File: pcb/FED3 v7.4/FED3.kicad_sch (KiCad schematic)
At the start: 29 parts, among them IC2 TB6612FNG, SW1 Sw, U2 MIC5504-3.3, U3 MCP73831T, X5 JST-XH-02

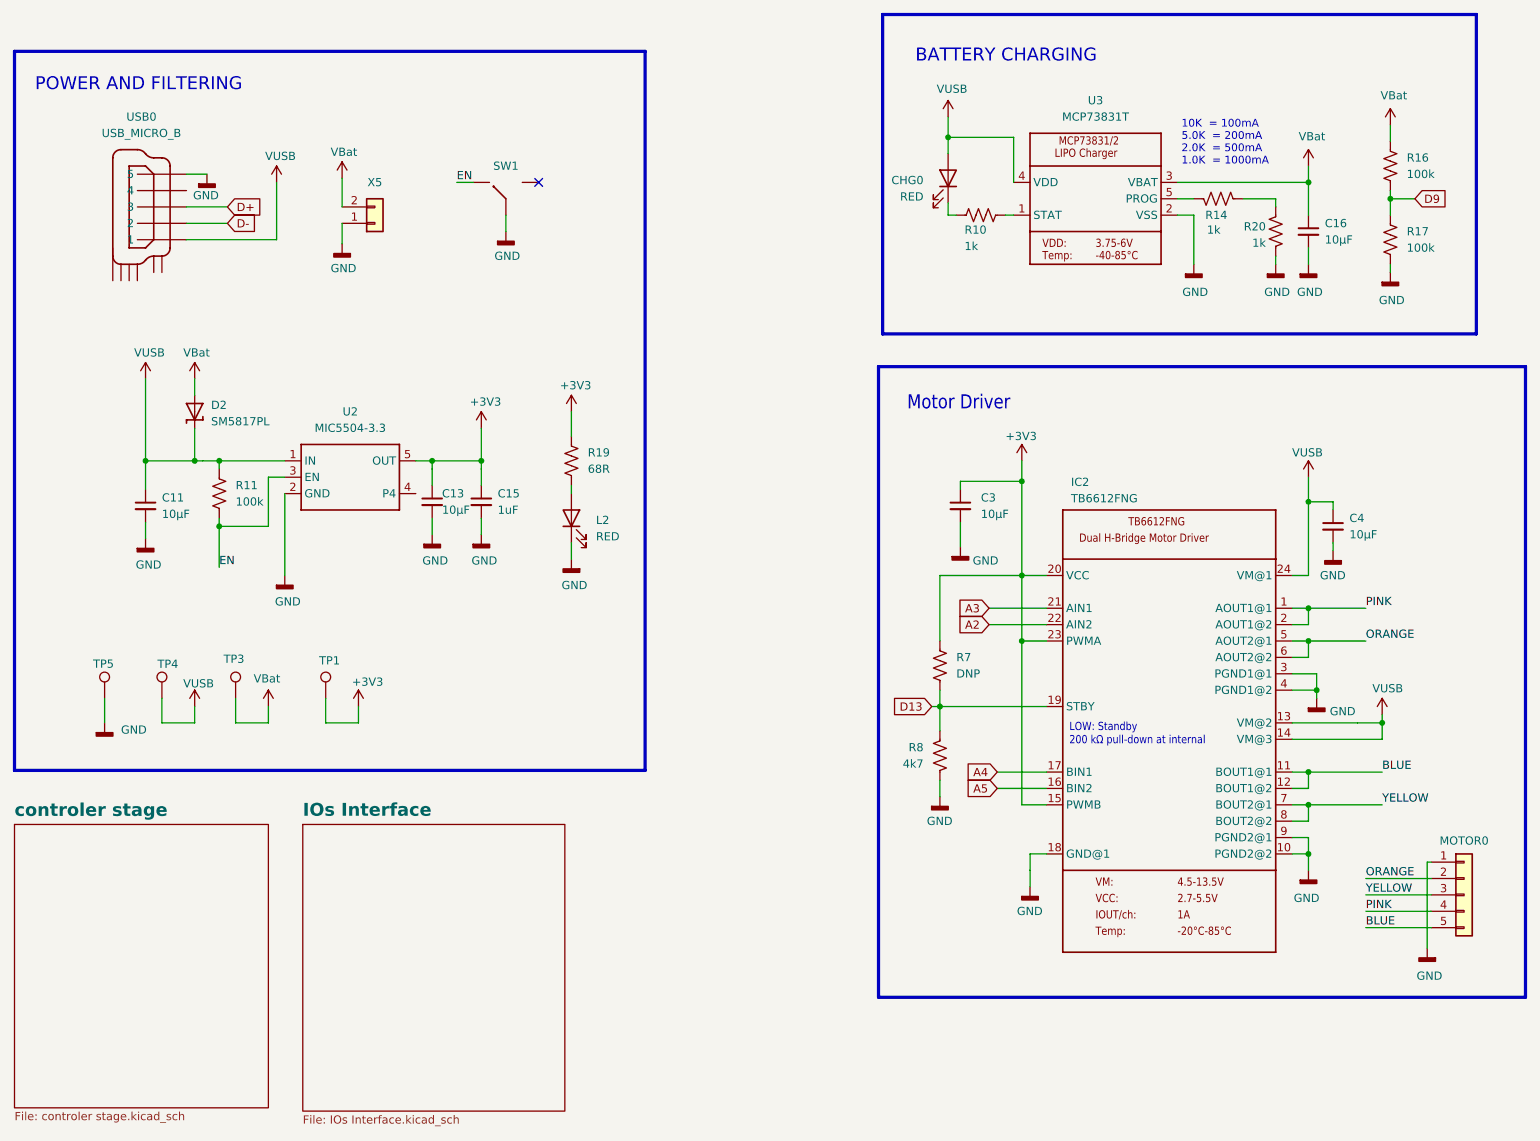
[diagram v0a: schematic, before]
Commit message: v.7.4 - alterações rail power
v.7.4
- modificada estrutura rail power: VUSB apenas para Vcharging
- modificadas Rs de LEDs para diminuir I
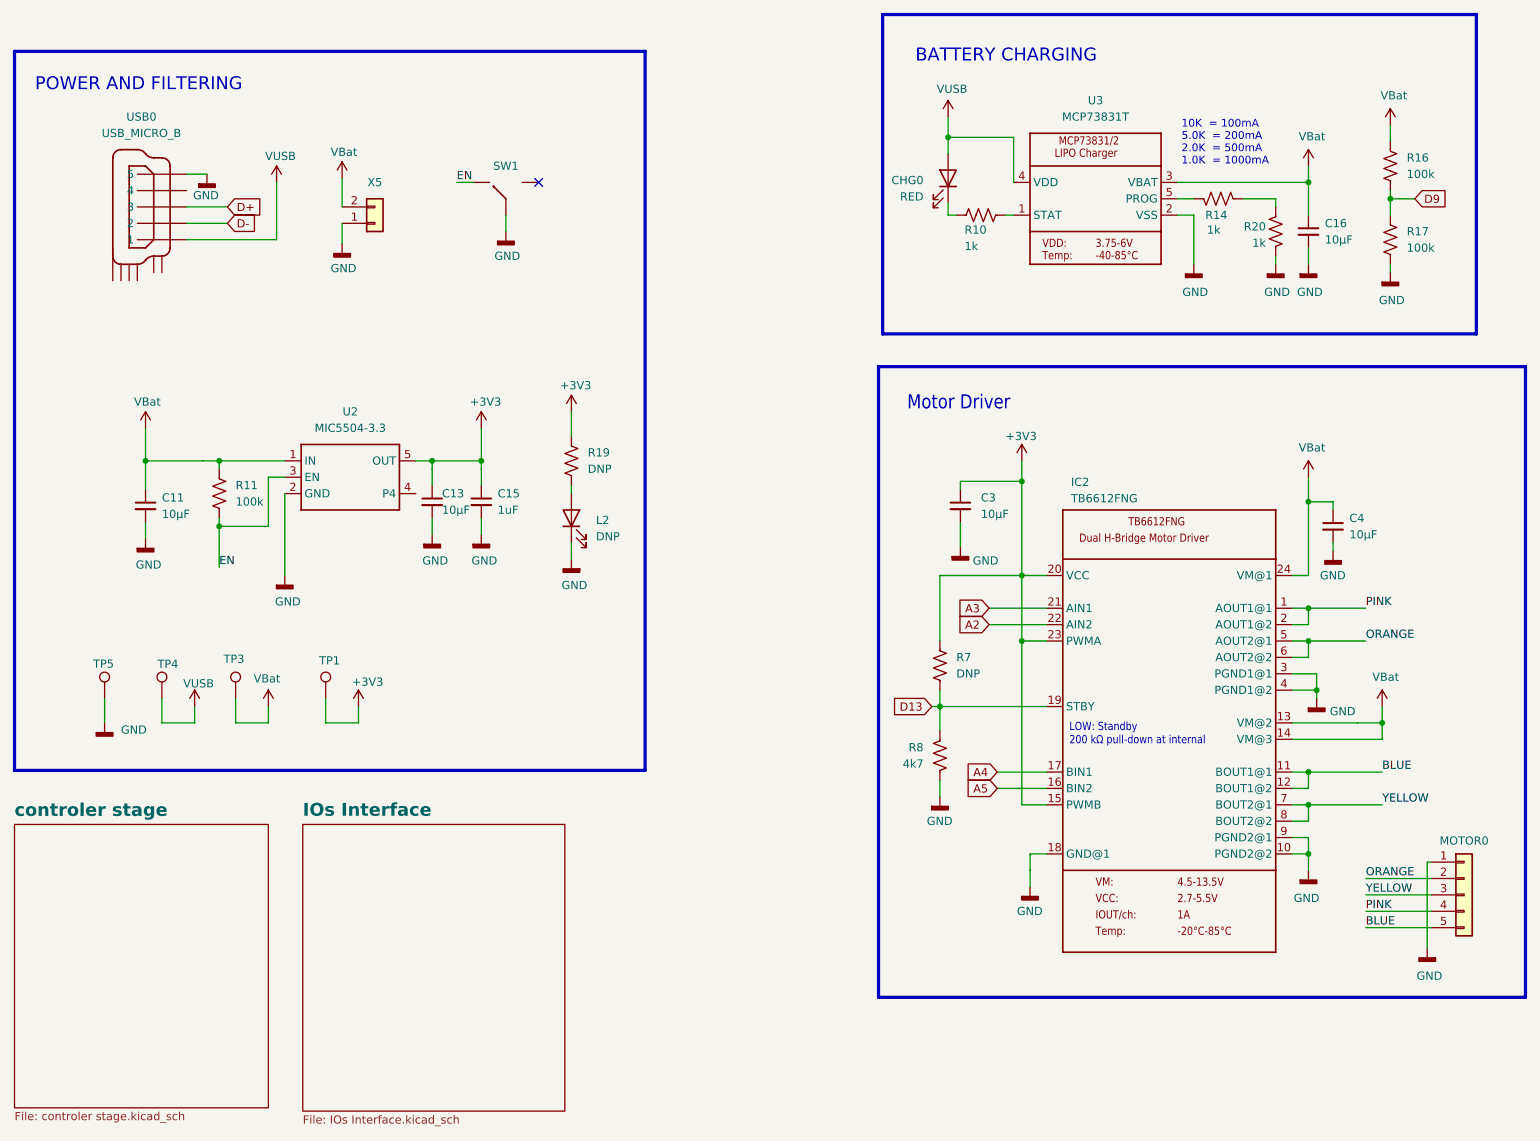
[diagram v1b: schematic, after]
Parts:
- removed D2: SM5817PL, Diode_SMD:D_SOD-123F, symbol FED3 SymbLib:DIODE-SCHOTTKYSOD-123
- L2: value RED -> DNP; MPN 5975004407F -> n.a.; OEPSPN OEPS030006 -> n.a.
- R16, R17: MPN ERJ-2RKF1003X -> RG1005P-104-B-T5; OEPSPN OEPS020019 -> OEPS020175
- R19: value 68R -> DNP; MPN RCS040268R0FKED -> n.a.; OEPSPN OEPS020032 -> n.a.; now left out of the parts list
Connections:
- net VBat: now also C11.1, C4.1, IC2.13 (VM@2), IC2.14 (VM@3), IC2.24 (VM@1), R11.1, U2.1 (IN)
- net VUSB: no longer C11.1, C4.1, IC2.13 (VM@2), IC2.14 (VM@3), IC2.24 (VM@1), R11.1, U2.1 (IN)

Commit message: v.7.4 - commit to final review
- I2C plug moved to board front side
- Rs to LEDs changed - impose less I
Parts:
- R11: MPN ERJ-2RKF1003X -> RG1005P-104-B-T5; OEPSPN OEPS020019 -> OEPS020175
- TP5: now left out of the parts list
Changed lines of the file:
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@@
 			)
 		)
-		(property "Description" ""
+		(property "Description" "SMD 0402 100kΩ ±0.1% 0.063W"
 			(at 58.42 88.9 0)
 			(effects
@@
 			)
 		)
-		(property "OEPSPN" "OEPS020019"
+		(property "OEPSPN" "OEPS020175"
 			(at 58.42 88.9 0)
 			(effects
@@
 			)
 		)
-		(property "MPN" "ERJ-2RKF1003X"
+		(property "MPN" "RG1005P-104-B-T5"
 			(at 58.42 88.9 0)
 			(effects
@@
 			)
 		)
-		(property "Description" ""
+		(property "Description" "LDO 3.3V 300mA"
 			(at 78.74 86.36 0)
 			(effects
@@
 			)
 		)
-		(property "Description" ""
+		(property "Description" "SMD CER 0402 1uF 25V ±10% X5R"
 			(at 99.06 90.17 0)
 			(effects
@@
 			)
 		)
-		(property "Description" ""
+		(property "Description" "SMD 0402 1kΩ ±1% 0.100W"
 			(at 213.36 43.18 0)
 			(effects
@@
 		(unit 1)
 		(exclude_from_sim no)
-		(in_bom yes)
+		(in_bom no)
 		(on_board yes)
 		(dnp no)
@@
 			)
 		)
-		(property "Description" ""
+		(property "Description" "SMD 0402 4.7kΩ ±1% 0.100W"
 			(at 170.18 129.54 0)
 			(effects
@@
 			)
 		)
-		(property "Description" ""
+		(property "Description" "BATT CNTL LI-ION 1CEL"
 			(at 194.31 43.18 0)
 			(effects
@@
 			)
 		)
-		(property "Description" ""
+		(property "Description" "SWITCH SLIDE SPDT 0.3A 5V (OEPS K01 017)"
 			(at 102.87 40.64 0)
 			(effects
@@
 			)
 		)
-		(property "Description" ""
+		(property "Description" "SMD 0402 1kΩ ±1% 0.100W"
 			(at 222.25 48.26 0)
 			(effects
@@
 			)
 		)
-		(property "Description" ""
+		(property "Description" "MOTOR DRIVER 2.7V-5.5V (OEPS K01 002)"
 			(at 204.47 124.46 0)
 			(effects
@@
 			)
 		)
-		(property "Description" ""
+		(property "Description" "SMD 0402 100kΩ ±0.1% 0.063W"
 			(at 240.03 38.1 0)
 			(effects
@@
 			)
 		)
-		(property "Description" ""
+		(property "Description" "SMD 0402 1kΩ ±1% 0.100W"
 			(at 176.53 45.72 0)
 			(effects
@@
 			)
 		)
-		(property "Description" ""
+		(property "Description" "SMD 0402 100kΩ ±0.1% 0.063W"
 			(at 240.03 49.53 0)
 			(effects

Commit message: FED3 v7.3 - 2nd revision
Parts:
- L2, R7: now not fitted; now left out of the parts list
- R11, R16, R17: value 100k -> 100k 0.1%
- R19: now not fitted
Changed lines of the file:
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@@
 			)
 		)
-		(property "Value" "100k"
+		(property "Value" "100k 0.1%"
 			(at 60.96 90.1699 0)
 			(effects
@@
 		(unit 1)
 		(exclude_from_sim no)
-		(in_bom yes)
+		(in_bom no)
 		(on_board yes)
-		(dnp no)
+		(dnp yes)
 		(fields_autoplaced yes)
 		(property "Reference" "L2"
@@
 		(in_bom no)
 		(on_board yes)
-		(dnp no)
+		(dnp yes)
 		(fields_autoplaced yes)
 		(property "Reference" "R19"
@@
 			)
 		)
-		(property "Value" "100k"
+		(property "Value" "100k 0.1%"
 			(at 242.57 39.3699 0)
 			(effects
@@
 			)
 		)
-		(property "Value" "100k"
+		(property "Value" "100k 0.1%"
 			(at 242.57 50.7999 0)
 			(effects
@@
 		(unit 1)
 		(exclude_from_sim no)
-		(in_bom yes)
+		(in_bom no)
 		(on_board yes)
-		(dnp no)
+		(dnp yes)
 		(fields_autoplaced yes)
 		(property "Reference" "R7"

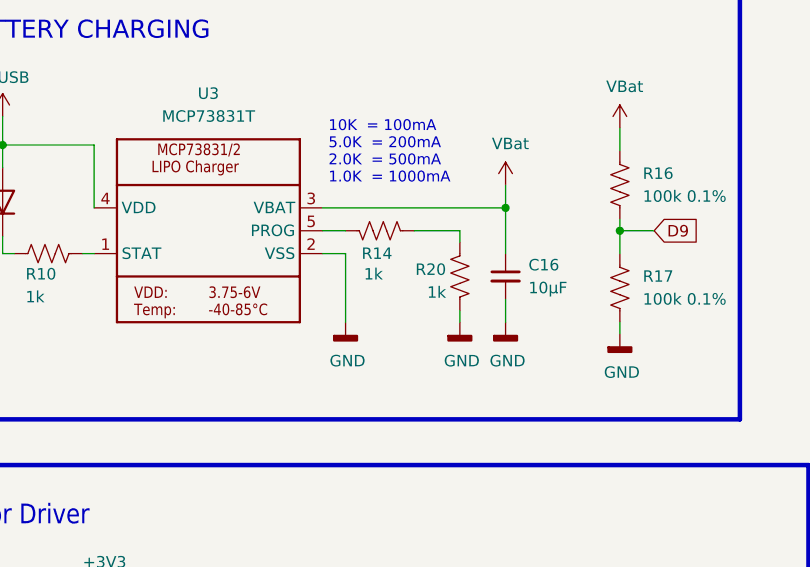
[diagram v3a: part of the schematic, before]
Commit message: modificados valores R14 R20: 2k2
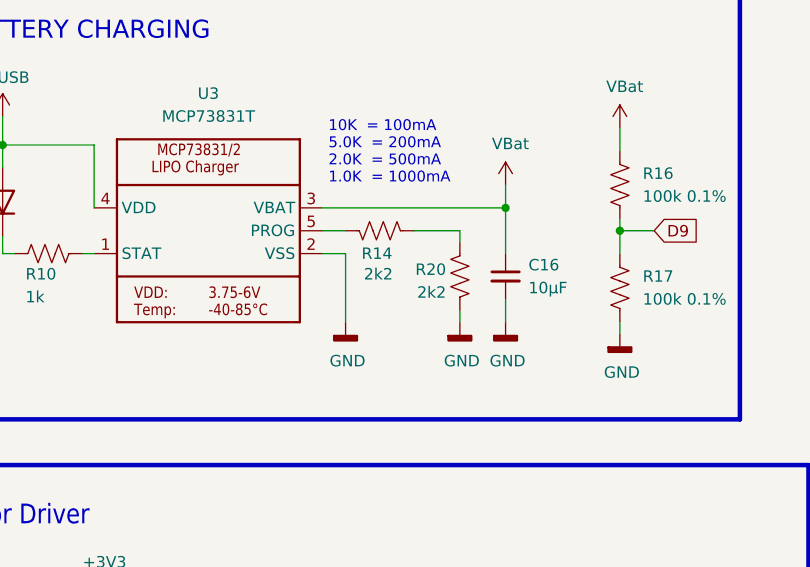
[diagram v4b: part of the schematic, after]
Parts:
- R14, R20: value 1k -> 2k2; MPN ERJ-2RKF1001X -> ERJ-2RKF2201X; OEPSPN OEPS020006 -> OEPS020174
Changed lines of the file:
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@@
 			)
 		)
-		(property "Value" "1k"
+		(property "Value" "2k2"
 			(at 211.582 48.006 90)
 			(effects
@@
 			)
 		)
-		(property "Description" "SMD 0402 1kΩ ±1% 0.100W"
+		(property "Description" "SMD 0402 2.2kΩ ±1% 0.100W"
 			(at 213.36 43.18 0)
 			(effects
@@
 			)
 		)
-		(property "OEPSPN" "OEPS020006"
+		(property "OEPSPN" "OEPS020174"
 			(at 213.36 43.18 0)
 			(effects
@@
 			)
 		)
-		(property "MPN" "ERJ-2RKF1001X"
+		(property "MPN" "ERJ-2RKF2201X"
 			(at 213.36 43.18 0)
 			(effects
@@
 			)
 		)
-		(property "Value" "1k"
+		(property "Value" "2k2"
 			(at 220.726 50.038 0)
 			(effects
@@
 			)
 		)
-		(property "Description" "SMD 0402 1kΩ ±1% 0.100W"
+		(property "Description" "SMD 0402 2.2kΩ ±1% 0.100W"
 			(at 222.25 48.26 0)
 			(effects
@@
 			)
 		)
-		(property "OEPSPN" "OEPS020006"
+		(property "OEPSPN" "OEPS020174"
 			(at 222.25 48.26 0)
 			(effects
@@
 			)
 		)
-		(property "MPN" "ERJ-2RKF1001X"
+		(property "MPN" "ERJ-2RKF2201X"
 			(at 222.25 48.26 0)
 			(effects

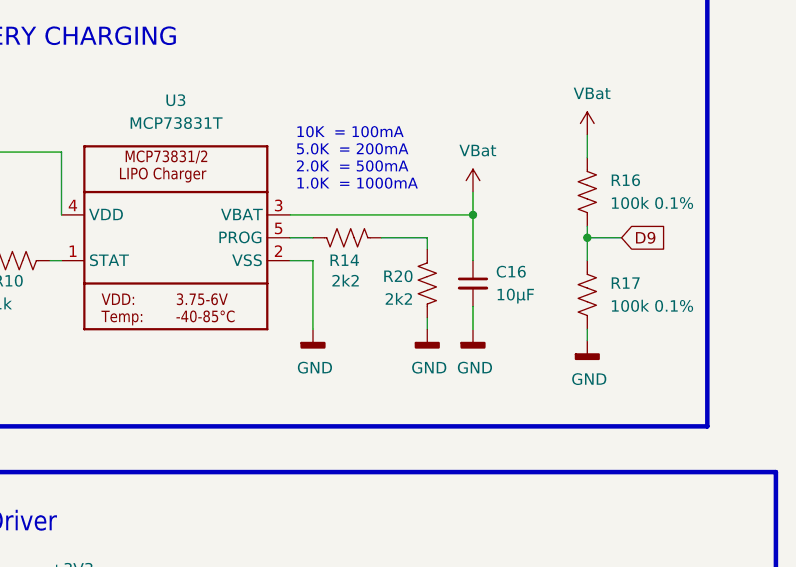
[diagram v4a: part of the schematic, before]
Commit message: R20 off; R14=2k2
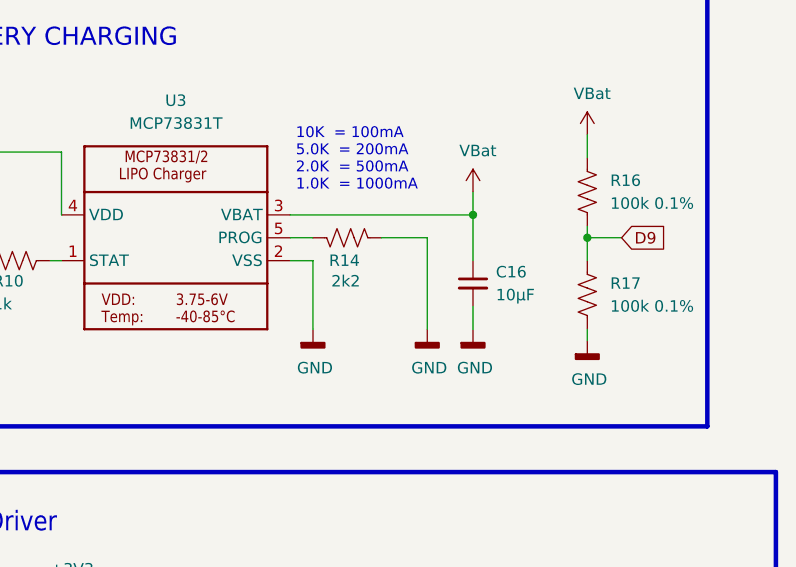
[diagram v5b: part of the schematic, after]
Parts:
- removed R20: 2k2, Resistor_SMD:R_0402_1005Metric, symbol Device:R_US
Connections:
- net GND: now also R14.1
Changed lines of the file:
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@@
 	(wire
 		(pts
-			(xy 222.25 44.45) (xy 222.25 43.18)
+			(xy 222.25 43.18) (xy 222.25 53.34)
 		)
 		(stroke
@@
 	(wire
 		(pts
-			(xy 222.25 52.07) (xy 222.25 53.34)
-		)
-		(stroke
-			(width 0)
-			(type solid)
-		)
-	)
-	(wire
-		(pts
 			(xy 224.79 134.62) (xy 227.33 134.62)
 		)
@@
 					(unit 1)
 				)
-			)
-		)
-	)
-	(symbol
-		(lib_id "Device:R_US")
-		(at 222.25 48.26 0)
-		(mirror x)
-		(unit 1)
-		(exclude_from_sim no)
-		(in_bom yes)
-		(on_board yes)
-		(dnp no)
-		(property "Reference" "R20"
-			(at 220.726 47.498 0)
-			(effects
-				(font
-					(size 1.27 1.27)
-				)
-				(justify right)
-			)
-		)
-		(property "Value" "2k2"
-			(at 220.726 50.038 0)
-			(effects
-				(font
-					(size 1.27 1.27)
-				)
-				(justify right)
-			)
-		)
-		(property "Footprint" "Resistor_SMD:R_0402_1005Metric"
-			(at 222.25 48.26 0)
-			(effects
-				(font
-					(size 1.27 1.27)
-				)
-				(hide yes)
-			)
-		)
-		(property "Datasheet" ""
-			(at 222.25 48.26 0)
-			(effects
-				(font
-					(size 1.27 1.27)
-				)
-				(hide yes)
-			)
-		)
-		(property "Description" "SMD 0402 2.2kΩ ±1% 0.100W"
-			(at 222.25 48.26 0)
-			(effects
-				(font
-					(size 1.27 1.27)
-				)
-				(hide yes)
-			)
-		)
-		(property "OEPSPN" "OEPS020174"
-			(at 222.25 48.26 0)
-			(effects
-				(font
-					(size 1.27 1.27)
-				)
-				(hide yes)
-			)
-		)
-		(property "MPN" "ERJ-2RKF2201X"
-			(at 222.25 48.26 0)
-			(effects
-				(font
-					(size 1.27 1.27)
-				)
-				(hide yes)
-			)
-		)
-		(pin "1"
-		)
-		(pin "2"
-		)
-		(instances
-			(project "FED3_v7.3"
-				(path "/2ba63f12-2fcd-4471-9636-2762cde37de8"
-					(reference "R20")
-					(unit 1)
-				)

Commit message: retomar sincronia PCB com main-branch @12Junho
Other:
- note added: "2.2K = 455mA"
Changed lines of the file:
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@@
 	(text "5.0K  = 200mA"
 		(exclude_from_sim no)
-		(at 207.645 34.29 0)
+		(at 207.772 32.385 0)
 		(effects
 			(font
@@
 		)
 	)
+	(text "2.2K  = 455mA"
+		(exclude_from_sim no)
+		(at 207.772 34.29 0)
+		(effects
+			(font
+				(size 1.2 1.2)
+			)
+			(justify left bottom)
+		)
+	)
 	(text "1.0K  = 1000mA"
 		(exclude_from_sim no)
@@
 	(text "10K  = 100mA"
 		(exclude_from_sim no)
-		(at 207.645 32.385 0)
+		(at 207.772 30.48 0)
 		(effects
 			(font

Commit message: actualizados ficheiros produção
- modificadas props de componentes para agilizar o criar ficheiros de produção
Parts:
- MOTOR0: now in the parts list
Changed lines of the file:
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@@
 		(unit 1)
 		(exclude_from_sim no)
-		(in_bom no)
+		(in_bom yes)
 		(on_board yes)
 		(dnp no)

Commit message: getting tunned with Jonathan review #13
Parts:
- MOTOR0: now left out of the parts list
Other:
- sheet controler stage renamed Controller Stage
- company: (none) -> Kravitz Lab
- title: (none) -> FED3 Control Board
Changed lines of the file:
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@@
 	(generator_version "9.0")
 	(paper "A4")
+	(title_block
+		(title "FED3 Control Board")
+		(rev "7.4")
+		(company "Kravitz Lab")
+		(comment 1 "Open Ephys, Inc.")
+	)
 	(rectangle
 		(start 161.29 14.605)
@@
 		(unit 1)
 		(exclude_from_sim no)
-		(in_bom yes)
+		(in_bom no)
 		(on_board yes)
 		(dnp no)
@@
 			(color 202 239 212 1.0000)
 		)
-		(property "Sheetname" "controler stage"
+		(property "Sheetname" "Controller Stage"
 			(at 26.67 139.1314 0)
 			(effects
@@
 	)
 	(embedded_fonts no)
+	(embedded_files
+		(file
+			(name "generic.kicad_wks")
+			(type worksheet)
+			(data |KLUv/WDdCX0VAPbdXiHwth4UjMf84wQpaKiddXNyw2vE3ASpJOKm/UZkMyvPewFVAE4AWAA71P+6
+				E/V/PHhP6hl7NhdyvnNBg6Vy+uc/TLoZgwYrqd8THr90vwAABASi6O845VVxKvxdDihWvvVz++br
+				MViUUkSd1bPG476jAiAgGEMkzsd5OFQI1UctVrTy7u1E2OrTmkrby9ifu+L1uW/e2nvQp88q5Gmw
+				8ws+fr+f9y+L9Oa88s83DLU3p1VMWf3Lt9ZppVX9shLSUuq/uR+rym/I5fdulhPePlB3nqiaJruM
+				7sWyKo9QmUhQSqlo2yXTcBxYQ4ugCHXaOS+p8GvKeqUyDObgZJlt01AEZ9znHHtv076fr+emDv5R
+				BLLVKWaq1mfXdZMiCoDPukPdBgGBofrisvaiijoRFEPJJqbMiaFuzLqhYJZJpTHlApNlkM2yEDIx
+				wSiZRHvgh4dB7rEbqteFnDSTYDQM+BhzSVrph/3v/WyDQ2rwaZU/F27d8X1FznLJLFiAhKDhRMcY
+				khEJkiRJOnBEpOSqG67IIUSIB6wVkypOj83iBj0zp4LL2kMMw+lEgMAIPplQr3guKCdlw/SfU9Pm
+				wv5Qjf2c0i+iukyGwJWg6H+jq3g9lh1bbaelmbDHUSOcHe0f4IqIU3pYnNopN2UGuqm6tUzbD0DL
+				A846XZ/tXUnW1CdqEKGhzI4PDvNZEWdNQVTqjKoxCJiOkLlyPnE2aN0Mgntwtl4Il0TKJW3CO+mz
+				Z3UY05BTT9QUnWnIY2O5jqbO0VBDfwAQ0J2lPShW8OIwbtD7c16HHQWSRlikdRdv3bO2EHlrLTcN
+				okDmqiZIAfyy8oU9FMxL3Rl0kbp+k4D31UmB0+QSWL73QeUaK7tJbNu8DHaE+JnfMeyjQJuerxNn
+				/RsMH2E/mWuAPwa9Cg==|
+			)
+			(checksum "29ED9DE70340A48902A32D9A43F096A1")
+		)
+	)
 )
